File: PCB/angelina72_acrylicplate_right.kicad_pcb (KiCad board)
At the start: 2 copper layers, 162.3 x 124.6 mm, 25 parts, among them U1 ProMicro

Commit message: Update acrylic case
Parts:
- moved REF** 34.5 mm to (160.3, 142.8)
- moved REF** 9.26 mm to (51.3, 122.5), turned to 110 degrees
- moved REF** 4.29 mm to (199.7, 160.7)
- moved REF** 4.29 mm to (193.7, 40.3)
- moved REF** 4.29 mm to (38.0, 46.3)

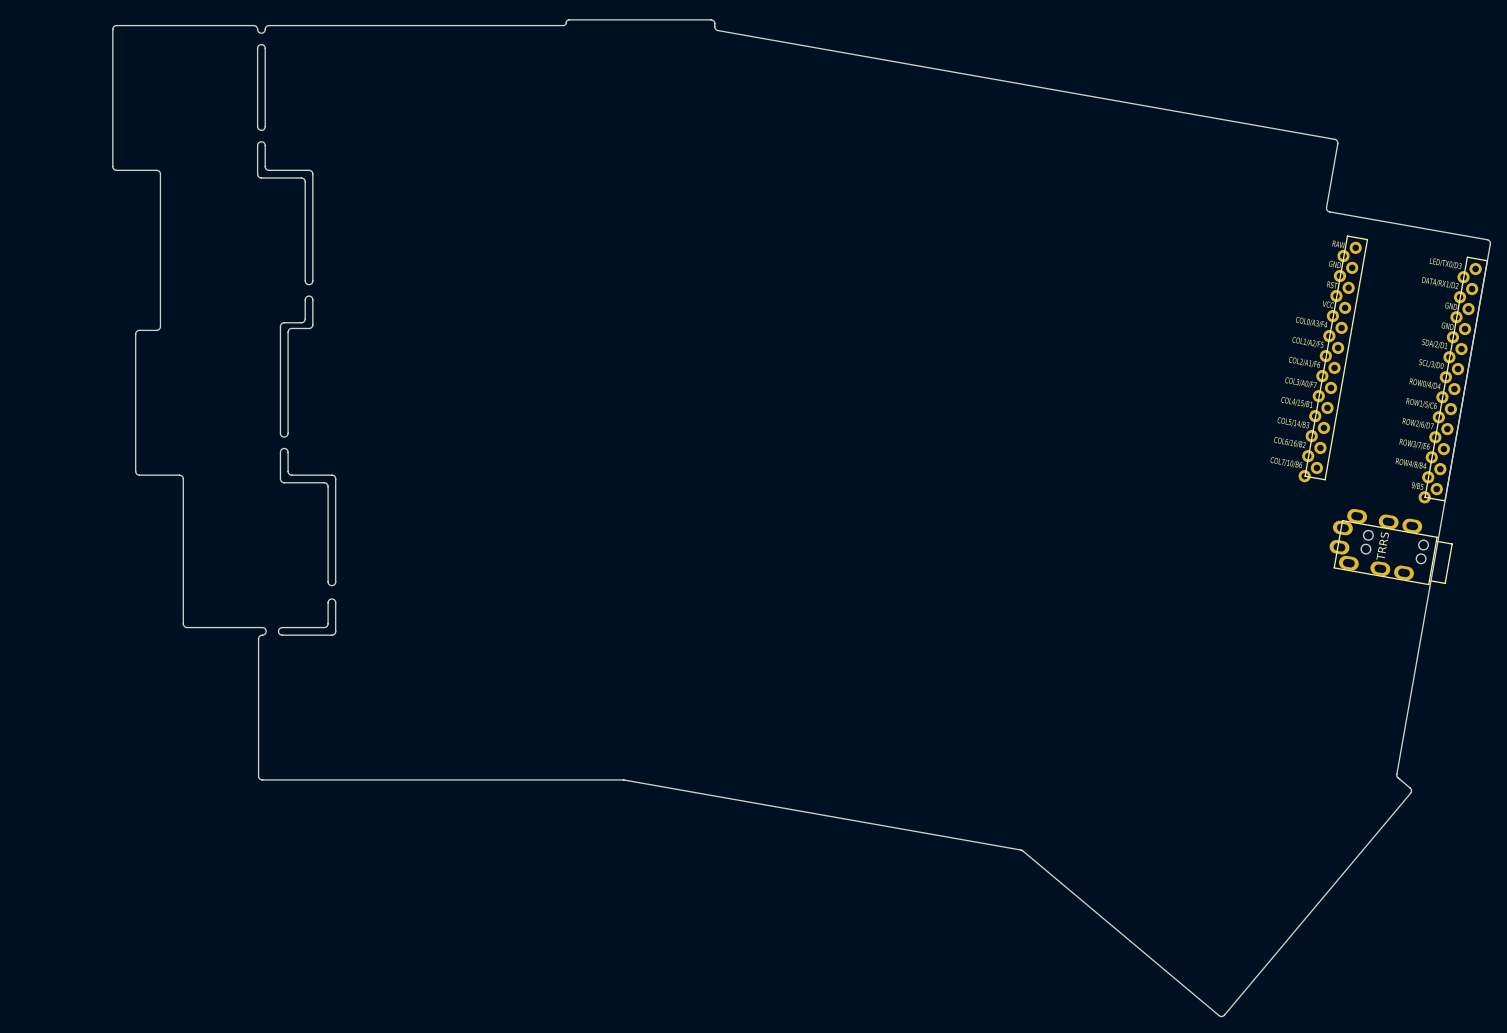
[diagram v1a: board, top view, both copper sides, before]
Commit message: PCBの空きレイヤーでscad用のポリゴンを書いた
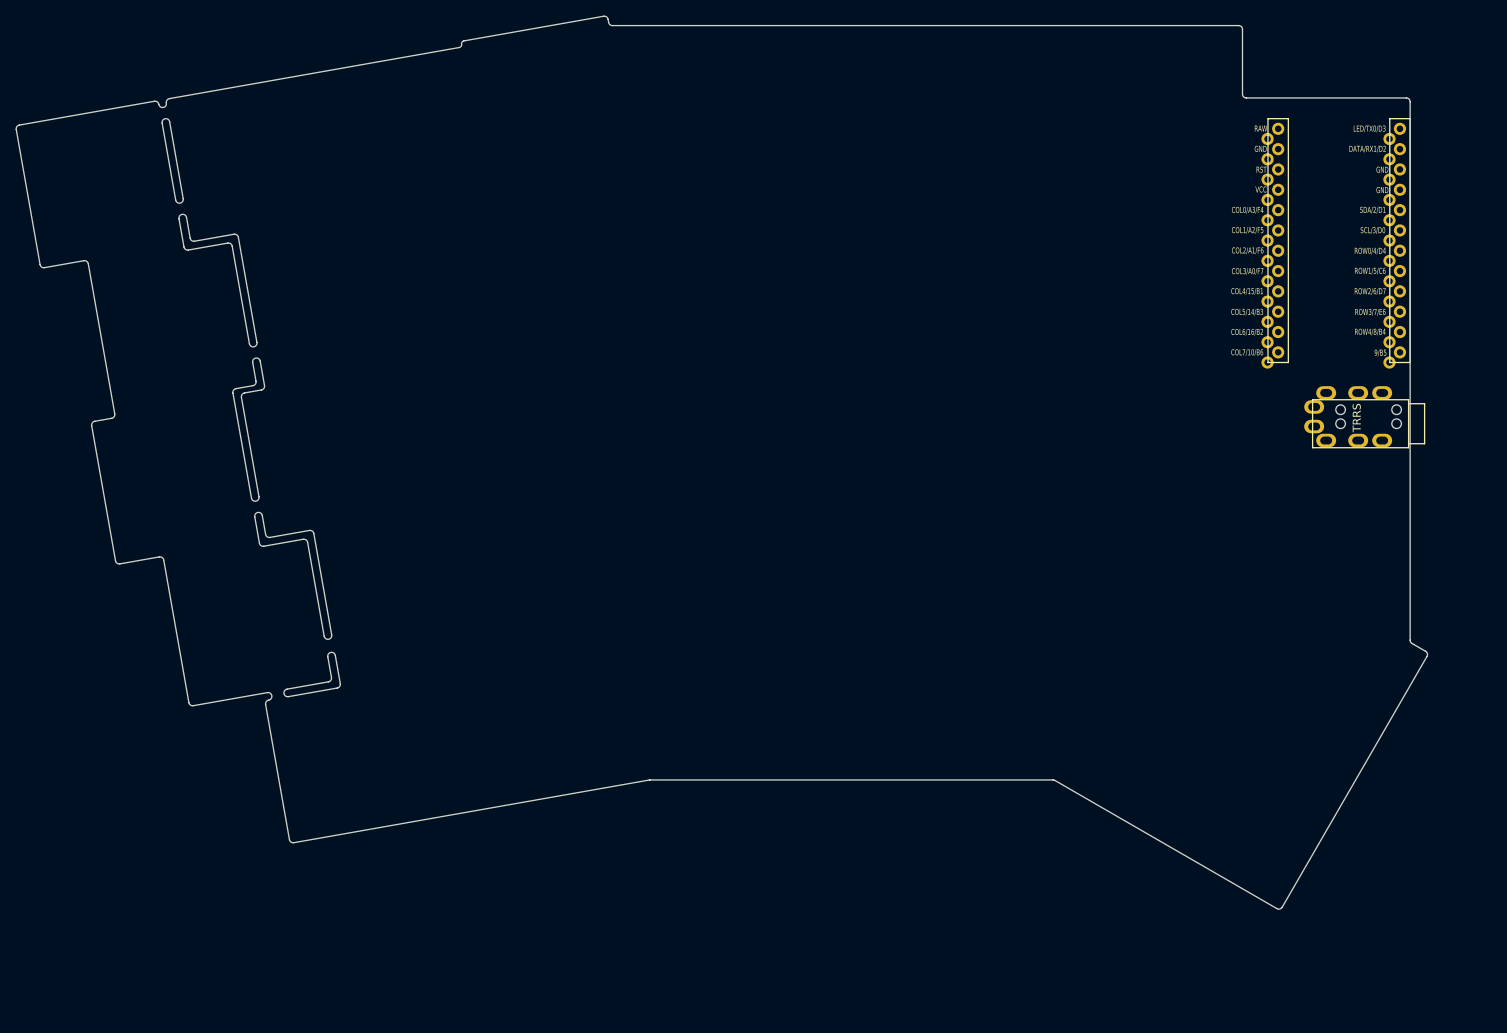
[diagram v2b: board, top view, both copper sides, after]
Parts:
- removed the REF** at (63.3, 134.2)
- removed the REF** at (216.9, 96.9)
- removed the REF** at (160.3, 142.8)
- removed the REF** at (45.1, 34.6)
- removed the REF** at (51.3, 122.5)
- removed the REF** at (214.5, 110.5)
- removed the REF** at (193.7, 40.3)
- removed the REF** at (199.7, 160.7)
- removed the REF** at (204.0, 49.4)
- removed the REF** at (223.0, 62.0)
- added REF**: MJ-19_3.5mm, angelina72:MJ-19_3.5mm, F.Cu at (219.1, 85.3)
- added REF**: M2_AcrylicHole, angelina72:M2_AcrylicHole, F.Cu at (31.7, 47.1)
- added REF**: M5_AcrylicHole, angelina72:M5_AcrylicHole, F.Cu at (179.7, 26.5)
- added REF**: M2_AcrylicHole, angelina72:M2_AcrylicHole, F.Cu at (191.8, 33.9)
- added REF**: M5_AcrylicHole, angelina72:M5_AcrylicHole, F.Cu at (207.6, 145.2)
- added REF**: M2_AcrylicHole, angelina72:M2_AcrylicHole, F.Cu at (69.0, 143.0)
- added REF**: M2_AcrylicHole, angelina72:M2_AcrylicHole, F.Cu at (112.3, 33.9)
- added REF**: M5_AcrylicHole, angelina72:M5_AcrylicHole, F.Cu at (56.8, 132.6)
- added REF**: M2_AcrylicHole, angelina72:M2_AcrylicHole, F.Cu at (194.9, 152.4)
- added REF**: M2_AcrylicHole, angelina72:M2_AcrylicHole, F.Cu at (212.3, 43.4)
- added REF**: M2_AcrylicHole, angelina72:M2_AcrylicHole, F.Cu at (115.1, 134.9)
- added REF**: M2_AcrylicHole, angelina72:M2_AcrylicHole, F.Cu at (212.5, 77.6)
- added REF**: M2_AcrylicHole, angelina72:M2_AcrylicHole, F.Cu at (212.5, 92.8)
- added REF**: M2_AcrylicHole, angelina72:M2_AcrylicHole, F.Cu at (164.5, 134.9)
- added REF**: M2_AcrylicHole, angelina72:M2_AcrylicHole, F.Cu at (212.3, 122.4)
- added SW10: KEY_SWITCH, angelina72:Outline_MXCherry_1u, F.Cu at (83.6, 50.5)
- added SW11: KEY_SWITCH, angelina72:Outline_MXCherry_1u, F.Cu at (92.8, 68.2)
- added SW12: KEY_SWITCH, angelina72:Outline_MXCherry_1u, F.Cu at (93.0, 87.5)
- added SW13: KEY_SWITCH, angelina72:Outline_MXCherry_1u, F.Cu at (102.2, 105.2)
- added SW14: KEY_SWITCH, angelina72:Outline_MXCherry_1u, F.Cu at (100.8, 124.8)
- added SW15: KEY_SWITCH, angelina72:Outline_MXCherry_1u, F.Cu at (102.2, 46.5)
- added SW16: KEY_SWITCH, angelina72:Outline_MXCherry_1u, F.Cu at (113.2, 65.3)
- added SW17: KEY_SWITCH, angelina72:Outline_MXCherry_1u, F.Cu at (113.2, 84.4)
- added SW18: KEY_SWITCH, angelina72:Outline_MXCherry_1u, F.Cu at (122.7, 103.4)
- added SW19: KEY_SWITCH, angelina72:Outline_MXCherry_1.25u, F.Cu at (125.1, 122.5)
- added SW20: KEY_SWITCH, angelina72:Outline_MXCherry_1u, F.Cu at (122.7, 46.3)
- added SW21: KEY_SWITCH, angelina72:Outline_MXCherry_1u, F.Cu at (132.3, 65.3)
- added SW22: KEY_SWITCH, angelina72:Outline_MXCherry_1u, F.Cu at (132.3, 84.4)
- added SW23: KEY_SWITCH, angelina72:Outline_MXCherry_1u, F.Cu at (141.8, 103.4)
- added SW24: KEY_SWITCH, angelina72:Outline_MXCherry_1.25u, F.Cu at (148.9, 122.5)
- added SW25: KEY_SWITCH, angelina72:Outline_MXCherry_1u, F.Cu at (141.8, 46.3)
- added SW26: KEY_SWITCH, angelina72:Outline_MXCherry_1u, F.Cu at (151.3, 65.3)
- added SW27: KEY_SWITCH, angelina72:Outline_MXCherry_1u, F.Cu at (151.3, 84.4)
- added SW28: KEY_SWITCH, angelina72:Outline_MXCherry_1u, F.Cu at (160.8, 103.4)
- added SW29: KEY_SWITCH, angelina72:Outline_MXCherry_1u, F.Cu at (160.8, 46.3)
- added SW30: KEY_SWITCH, angelina72:Outline_MXCherry_1u, F.Cu at (170.4, 65.3)
- added SW31: KEY_SWITCH, angelina72:Outline_MXCherry_1u, F.Cu at (170.4, 84.4)
- added SW32: KEY_SWITCH, angelina72:Outline_MXCherry_1u, F.Cu at (179.9, 103.4)
- added SW33: KEY_SWITCH, angelina72:Outline_MXCherry_1u, F.Cu at (173.9, 126.0)
- added SW34: KEY_SWITCH, angelina72:Outline_MXCherry_1u, F.Cu at (179.9, 46.3)
- added SW35: KEY_SWITCH, angelina72:Outline_MXCherry_1u, F.Cu at (199.9, 119.0)
- added SW36: KEY_SWITCH, angelina72:Outline_MXCherry_1u, F.Cu at (190.4, 135.5)
- added SW5: KEY_SWITCH, angelina72:Outline_MXCherry_1u, F.Cu at (46.1, 57.1)
- added SW5: KEY_SWITCH, angelina72:Outline_MXCherry_1u, F.Cu at (64.8, 53.8)
- added SW6: KEY_SWITCH, angelina72:Outline_MXCherry_1u, F.Cu at (55.2, 74.8)
- added SW6: KEY_SWITCH, angelina72:Outline_MXCherry_1u, F.Cu at (74.0, 71.5)
- added SW7: KEY_SWITCH, angelina72:Outline_MXCherry_1u, F.Cu at (55.5, 94.1)
- added SW7: KEY_SWITCH, angelina72:Outline_MXCherry_1u, F.Cu at (74.3, 90.8)
- added SW8: KEY_SWITCH, angelina72:Outline_MXCherry_1u, F.Cu at (64.7, 111.8)
- added SW8: KEY_SWITCH, angelina72:Outline_MXCherry_1u, F.Cu at (83.4, 108.5)
- added SW9: KEY_SWITCH, angelina72:Outline_MXCherry_1.25u, F.Cu at (79.7, 128.5)
- moved U1 17.5 mm to (201.0, 64.6), turned to 0 degrees
- moved J* 16.4 mm to (203.7, 87.0), turned to 270 degrees
- moved REF** 16.3 mm to (204.9, 93.9), turned to 0 degrees
- moved REF** 16.3 mm to (206.3, 107.0), turned to 0 degrees
- moved REF** 14.7 mm to (31.8, 59.6), turned to 100 degrees
- moved REF** 14.6 mm to (192.5, 86.1), turned to 0 degrees
- moved REF** 14.2 mm to (170.4, 55.1), turned to 10 degrees
- moved REF** 13.0 mm to (57.0, 64.1), turned to 10 degrees
- moved REF** 12.9 mm to (186.9, 122.5), turned to 330 degrees
- moved REF** 10.1 mm to (112.6, 54.7), turned to 10 degrees (x2)
- moved REF** 6.64 mm to (75.6, 118.8), turned to 10 degrees
- moved REF** 4.16 mm to (137.0, 114.0), turned to 10 degrees
- turned REF** to 0 degrees (x2)
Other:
- board size 162.3 x 124.6 mm -> 176.4 x 111.6 mm
